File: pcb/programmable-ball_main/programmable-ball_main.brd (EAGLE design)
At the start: 30.5 x 30.8 mm, 2 parts, among them J1 USB4125-GF-A_REVA2, U1 MDBT50Q-1MV2

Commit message: 軽微な修正
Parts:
- J1: value USB4125-GF-A_REVA2 -> USB4056-03-A_REVA2; device USB4125-GF-A_REVA2:GCT_USB4125-GF-A_REVA2 -> USB4056-03-A_REVA2:GCT_USB4056-03-A_REVA2
- moved J1 1.10 mm to (15.0, 2.00)
- moved U1 1.00 mm to (15.0, 19.0)
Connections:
- new net GND_A: J1.A1, J1.A12
- new net GND_B: J1.B1, J1.B12
- new net SHELL_GND: J1.S1, J1.S2, J1.S3, J1.S4
- new net USBD+: U1.35
- new net USBD-: U1.34
- new net VBUS_A: J1.A4, J1.A9
- new net VBUS_B: J1.B4, J1.B9
- net GND: no longer J1.A12, J1.B12
- net VBUS: no longer J1.A9, J1.B9
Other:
- board size 30.5 x 30.8 mm -> 40 x 40 mm
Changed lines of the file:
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@@
 <board>
 <plain>
-<wire x1="0" y1="0" x2="30.51" y2="0" width="0" layer="20"/>
-<wire x1="0" y1="30.77" x2="0" y2="0" width="0" layer="20"/>
+<wire x1="0" y1="30.77" x2="-2" y2="33" width="0" layer="20"/>
 <dimension x1="0" y1="0" x2="0" y2="30" x3="-6" y3="15" textsize="1.778" layer="47"/>
 <dimension x1="0" y1="0" x2="30" y2="0" x3="15" y3="-6" textsize="1.778" layer="47"/>
-<circle x="15" y="15" radius="15" width="0.1524" layer="20"/>
+<circle x="14" y="16" radius="20" width="1" layer="20"/>
+<circle x="4" y="16" radius="1" width="0.1524" layer="20"/>
+<circle x="5" y="11" radius="2.828425" width="0.1524" layer="20"/>
+<circle x="7" y="18" radius="1" width="0.1524" layer="20"/>
+<circle x="4" y="23" radius="1" width="0.1524" layer="20"/>
+<circle x="5" y="20" radius="1" width="0.1524" layer="20"/>
+<circle x="24" y="23" radius="1.4142125" width="0.1524" layer="20"/>
 </plain>
 <attributes>
@@
 </autorouter>
 <elements>
-<element name="U1" library="MDBT50Q-1MV2" package="XCVR_MDBT50Q-1MV2" value="MDBT50Q-1MV2" x="15" y="18" smashed="yes">
-<attribute name="AVAILABILITY" value="In Stock" x="15" y="18" size="1.778" layer="27" display="off"/>
-<attribute name="CHECK_PRICES" value="https://www.snapeda.com/parts/MDBT50Q-1MV2/Raytac+Corporation/view-part/?ref=eda" x="15" y="18" size="1.778" layer="27" display="off"/>
-<attribute name="DESCRIPTION" value=" 802.15.4, Bluetooth Bluetooth v5.2, Zigbee® Transceiver Module 2.36GHz ~ 2.5GHz Integrated, Chip Surface Mount " x="15" y="18" size="1.778" layer="27" display="off"/>
-<attribute name="MF" value="Raytac Corporation" x="15" y="18" size="1.778" layer="27" display="off"/>
-<attribute name="MP" value="MDBT50Q-1MV2" x="15" y="18" size="1.778" layer="27" display="off"/>
-<attribute name="NAME" x="9.75" y="26.19" size="1.27" layer="25"/>
-<attribute name="PACKAGE" value="SMD-61 Raytac Corporation" x="15" y="18" size="1.778" layer="27" display="off"/>
-<attribute name="PRICE" value="None" x="15" y="18" size="1.778" layer="27" display="off"/>
-<attribute name="SNAPEDA_LINK" value="https://www.snapeda.com/parts/MDBT50Q-1MV2/Raytac+Corporation/view-part/?ref=snap" x="15" y="18" size="1.778" layer="27" display="off"/>
+<element name="U1" library="MDBT50Q-1MV2" package="XCVR_MDBT50Q-1MV2" value="MDBT50Q-1MV2" x="15" y="19" smashed="yes">
+<attribute name="AVAILABILITY" value="In Stock" x="15" y="19" size="1.778" layer="27" display="off"/>
+<attribute name="CHECK_PRICES" value="https://www.snapeda.com/parts/MDBT50Q-1MV2/Raytac+Corporation/view-part/?ref=eda" x="15" y="19" size="1.778" layer="27" display="off"/>
+<attribute name="DESCRIPTION" value=" 802.15.4, Bluetooth Bluetooth v5.2, Zigbee® Transceiver Module 2.36GHz ~ 2.5GHz Integrated, Chip Surface Mount " x="15" y="19" size="1.778" layer="27" display="off"/>
+<attribute name="MF" value="Raytac Corporation" x="15" y="19" size="1.778" layer="27" display="off"/>
+<attribute name="MP" value="MDBT50Q-1MV2" x="15" y="19" size="1.778" layer="27" display="off"/>
+<attribute name="NAME" x="9.75" y="27.19" size="1.27" layer="25"/>
+<attribute name="PACKAGE" value="SMD-61 Raytac Corporation" x="15" y="19" size="1.778" layer="27" display="off"/>
+<attribute name="PRICE" value="None" x="15" y="19" size="1.778" layer="27" display="off"/>
+<attribute name="SNAPEDA_LINK" value="https://www.snapeda.com/parts/MDBT50Q-1MV2/Raytac+Corporation/view-part/?ref=snap" x="15" y="19" size="1.778" layer="27" display="off"/>
 </element>
-<element name="J1" library="USB4125-GF-A_REVA2" package="GCT_USB4125-GF-A_REVA2" value="USB4125-GF-A_REVA2" x="15" y="3.1" smashed="yes">
-<attribute name="DESCRIPTION" value=" USB Charge Only Connector Type C Horizontal Receptacle, 3.16mm profile, 6 Pins, Surface mount, Top mount, low cost " x="15" y="3.1" size="1.778" layer="27" display="off"/>
-<attribute name="DIGI-KEY_PART_NUMBER" value="2073-USB4125-GF-ATR-ND" x="15" y="3.1" size="1.778" layer="27" display="off"/>
-<attribute name="MF" value="Global Connector Technology" x="15" y="3.1" size="1.778" layer="27" display="off"/>
-<attribute name="MP" value="USB4125-GF-A" x="15" y="3.1" size="1.778" layer="27" display="off"/>
-<attribute name="NAME" x="11.7" y="7.6" size="1.27" layer="25"/>
-<attribute name="PACKAGE" value="None" x="15" y="3.1" size="1.778" layer="27" display="off"/>
-<attribute name="PURCHASE-URL" value="https://pricing.snapeda.com/search/part/USB4125-GF-A/?ref=eda" x="15" y="3.1" size="1.778" layer="27" display="off"/>
+<element name="J1" library="USB4056-03-A_REVA2" package="GCT_USB4056-03-A_REVA2" value="USB4056-03-A_REVA2" x="15" y="2" smashed="yes">
+<attribute name="AVAILABILITY" value="In Stock" x="15" y="2" size="1.778" layer="27" display="off"/>
+<attribute name="CHECK_PRICES" value="https://www.snapeda.com/parts/USB4056-03-A/Global+Connector+Technology/view-part/?ref=eda" x="15" y="2" size="1.778" layer="27" display="off"/>
+<attribute name="DESCRIPTION" value=" USB-C (USB TYPE-C) USB 3.2 Gen 2 (USB 3.1 Gen 2, Superspeed + (USB 3.1)) Receptacle Connector 24 Position Surface Mount, Right Angle; Through Hole " x="15" y="2" size="1.778" layer="27" display="off"/>
+<attribute name="MF" value="Global Connector Technology" x="15" y="2" size="1.778" layer="27" display="off"/>
+<attribute name="MP" value="USB4056-03-A" x="15" y="2" size="1.778" layer="27" display="off"/>
+<attribute name="PACKAGE" value="None" x="15" y="2" size="1.778" layer="27" display="off"/>
+<attribute name="PRICE" value="None" x="15" y="2" size="1.778" layer="27" display="off"/>
+<attribute name="SNAPEDA_LINK" value="https://www.snapeda.com/parts/USB4056-03-A/Global+Connector+Technology/view-part/?ref=snap" x="15" y="2" size="1.778" layer="27" display="off"/>
 </element>
 </elements>
@@
 <contactref element="U1" pad="33"/>
 <contactref element="U1" pad="2"/>
-<contactref element="J1" pad="B12"/>
-<contactref element="J1" pad="A12"/>
-<wire x1="10.35" y1="21.75" x2="19.65" y2="21.75" width="0" layer="19" extent="1-1"/>
-<wire x1="10.35" y1="20.65" x2="10.35" y2="21.75" width="0" layer="19" extent="1-1"/>
-<wire x1="10.2" y1="10.85" x2="10.35" y2="20.65" width="0" layer="19" extent="1-1"/>
-<wire x1="19.8" y1="10.85" x2="10.2" y2="10.85" width="0" layer="19" extent="1-1"/>
-<wire x1="17.75" y1="6.18" x2="10.2" y2="10.85" width="0" layer="19" extent="1-1"/>
-<wire x1="12.25" y1="6.18" x2="17.75" y2="6.18" width="0" layer="19" extent="1-1"/>
+<wire x1="10.35" y1="22.75" x2="19.65" y2="22.75" width="0" layer="19" extent="1-1"/>
+<wire x1="10.35" y1="21.65" x2="10.35" y2="22.75" width="0" layer="19" extent="1-1"/>
+<wire x1="10.2" y1="11.85" x2="10.35" y2="21.65" width="0" layer="19" extent="1-1"/>
+<wire x1="19.8" y1="11.85" x2="10.2" y2="11.85" width="0" layer="19" extent="1-1"/>
 </signal>
 <signal name="VDDH">
@@
 <signal name="VBUS">
 <contactref element="U1" pad="32"/>
-<contactref element="J1" pad="B9"/>
-<contactref element="J1" pad="A9"/>
-<wire x1="16.52" y1="6.18" x2="19" y2="10.85" width="0" layer="19" extent="1-1"/>
-<wire x1="13.48" y1="6.18" x2="16.52" y2="6.18" width="0" layer="19" extent="1-1"/>
 </signal>
 <signal name="DCCH">
@@
 <contactref element="U1" pad="28"/>
 </signal>
+<signal name="USBD+">
+<contactref element="U1" pad="35"/>
+</signal>
+<signal name="USBD-">
+<contactref element="U1" pad="34"/>
+</signal>
+<signal name="GND_A">
+<contactref element="J1" pad="A12"/>
+<contactref element="J1" pad="A1"/>
+<wire x1="17.75" y1="8.2" x2="12.25" y2="8.2" width="0" layer="19" extent="1-1"/>
+</signal>
+<signal name="VBUS_A">
+<contactref element="J1" pad="A4"/>
+<contactref element="J1" pad="A9"/>
+<wire x1="16.25" y1="8.2" x2="13.75" y2="8.2" width="0" layer="19" extent="1-1"/>
+</signal>
+<signal name="SHELL_GND">
+<contactref element="J1" pad="S2"/>
+<contactref element="J1" pad="S1"/>
+<contactref element="J1" pad="S4"/>
+<contactref element="J1" pad="S3"/>
+<wire x1="10.87" y1="6.4" x2="10.51" y2="2" width="0" layer="19" extent="1-1"/>
+<wire x1="19.13" y1="6.4" x2="10.87" y2="6.4" width="0" layer="19" extent="1-1"/>
+<wire x1="19.49" y1="2" x2="19.13" y2="6.4" width="0" layer="19" extent="1-1"/>
+</signal>
+<signal name="GND_B">
+<contactref element="J1" pad="B12"/>
+<contactref element="J1" pad="B1"/>
+<wire x1="17.8" y1="6.99" x2="12.2" y2="6.99" width="0" layer="19" extent="1-1"/>
+</signal>
+<signal name="VBUS_B">
+<contactref element="J1" pad="B9"/>
+<contactref element="J1" pad="B4"/>
+<wire x1="16.2" y1="6.99" x2="13.8" y2="6.99" width="0" layer="19" extent="1-1"/>
+</signal>
 </signals>

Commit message: usb typeC周り実装 #4
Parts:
- added R1, R2: 5.1k, SparkFun-Resistors:0402-TIGHT
- J1: value USB4056-03-A_REVA2 -> 12402012E212A; device USB4056-03-A_REVA2:GCT_USB4056-03-A_REVA2 -> 12402012E212A:AMPHENOL_12402012E212A
- moved J1 2.50 mm to (15.0, 4.50)
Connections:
- removed net GND_A: J1.A1, J1.A12
- removed net GND_B: J1.B1, J1.B12
- removed net SHELL_GND: J1.S1, J1.S2, J1.S3, J1.S4
- removed net VBUS_A: J1.A4, J1.A9
- removed net VBUS_B: J1.B4, J1.B9
- new net N$1: J1.A5, R1.2
- new net N$2: J1.B5, R2.2
- net GND: now also J1.A1_B12, J1.B1_A12, R1.1, R2.1
- net USBD+: now also J1.A6, J1.B6
- net USBD-: now also J1.A7, J1.B7
- net VBUS: now also J1.A4_B9, J1.B4_A9
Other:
- board size 40 x 40 mm -> 27 x 27 mm

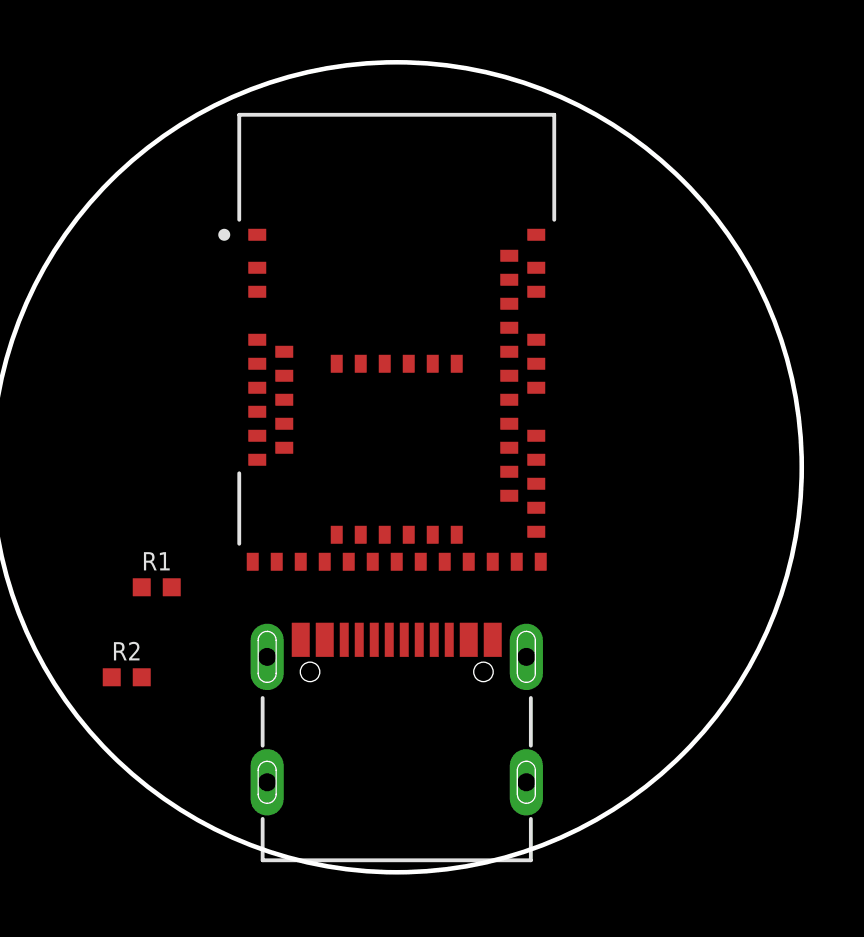
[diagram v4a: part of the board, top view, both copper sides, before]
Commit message: スイッチを追加 #4
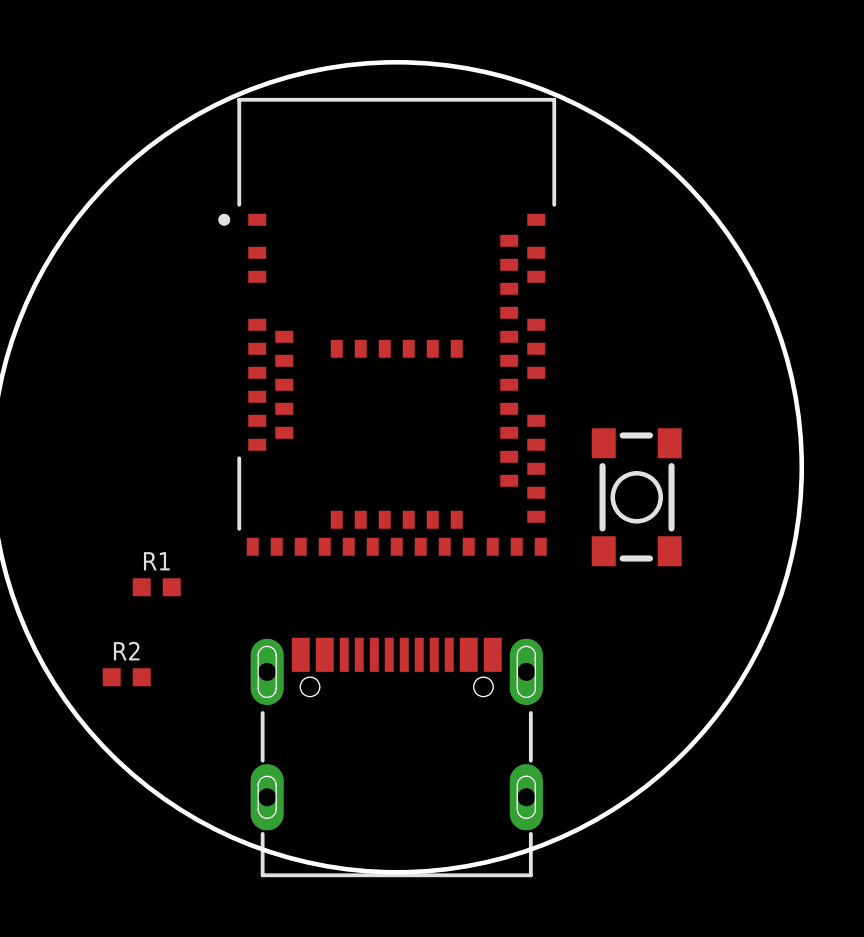
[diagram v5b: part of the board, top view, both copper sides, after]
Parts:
- added S1: SWITCH-MOMENTARY-SPSTSMD-3, SparkFun-Retired:TACTILE_SWITCH_SMD-3
- moved J1 0.50 mm to (15.0, 4.00)
- moved U1 0.50 mm to (15.0, 19.5)
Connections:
- new net I2C_SCL: U1.49
- new net I2C_SDA: U1.19
- new net RESET: S1.4, U1.40
- new net SWDCLK: U1.53
- new net SWDIO: U1.51
- net GND: now also S1.1

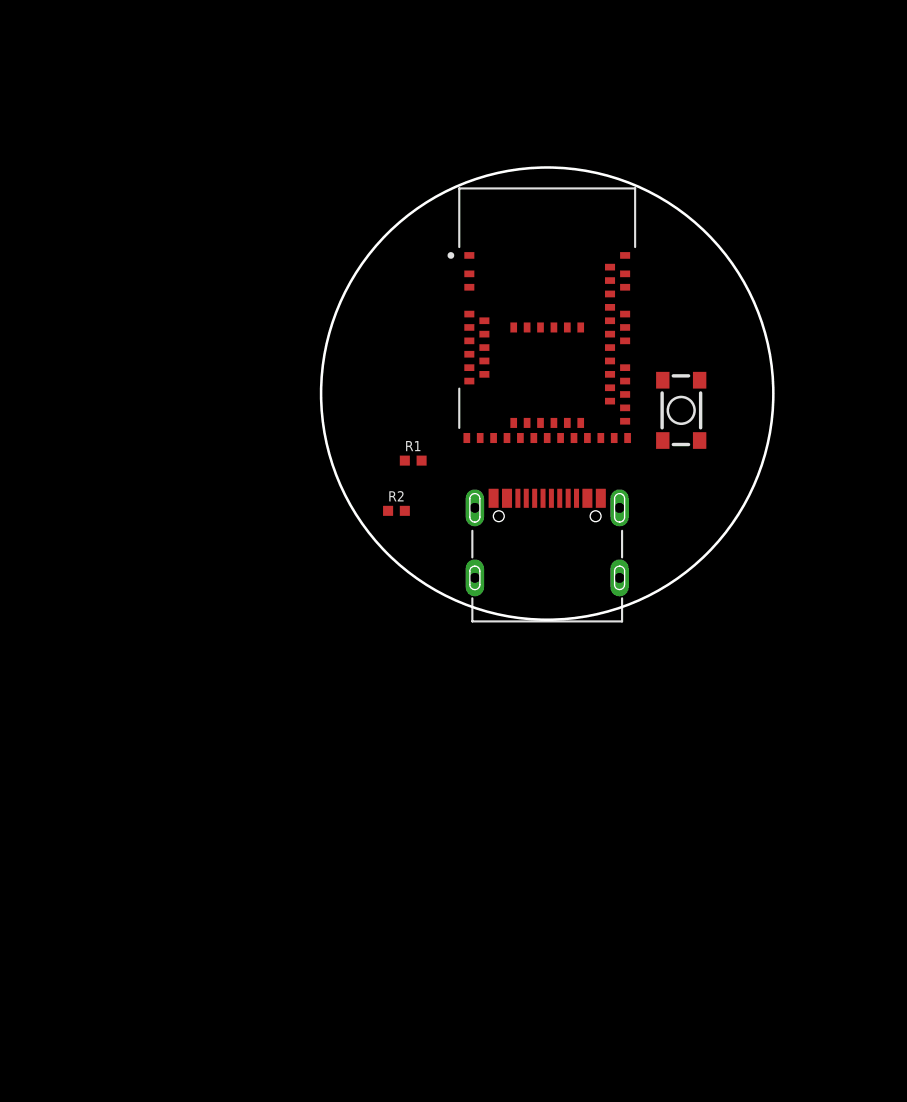
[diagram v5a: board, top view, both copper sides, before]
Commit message: 3.3VのレギュレータとVBATよりVBUSを優先するように修正
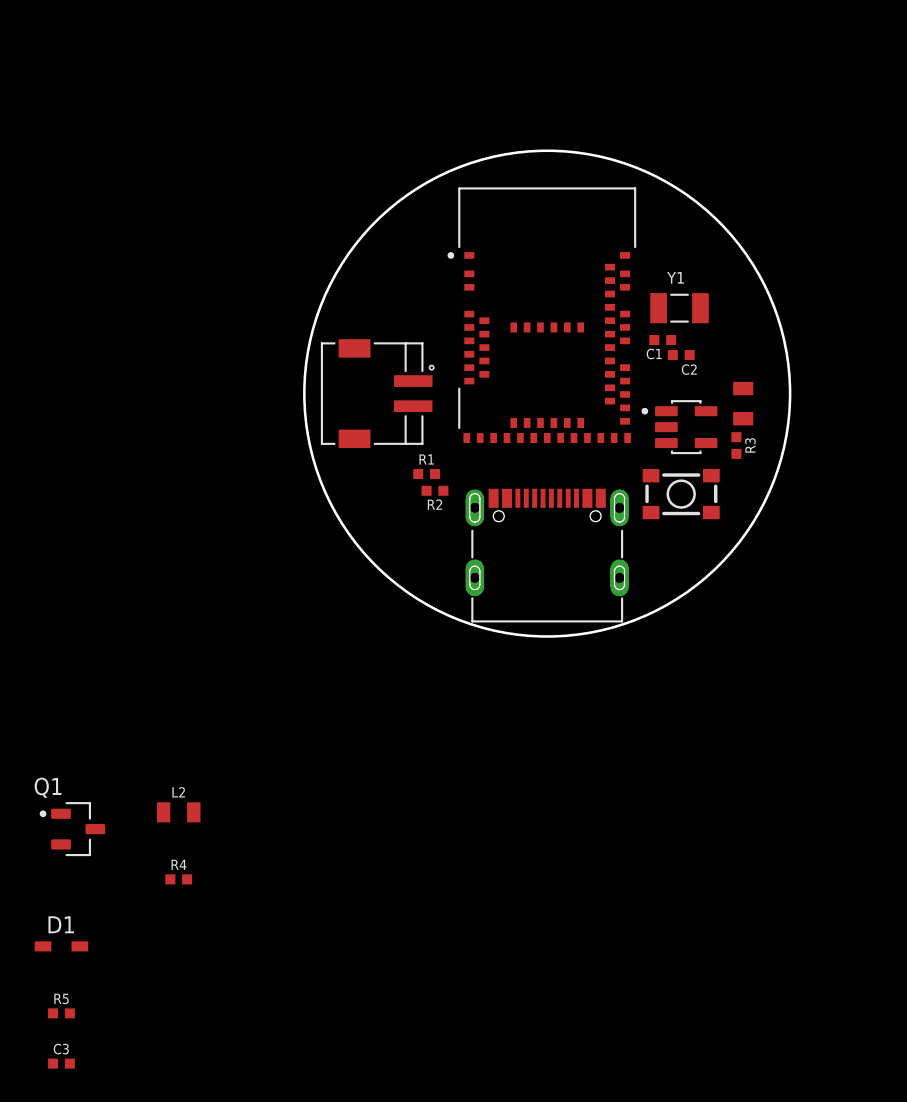
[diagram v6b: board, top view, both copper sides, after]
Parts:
- added C1, C2: 9.1pF, SparkFun-Capacitors:0402-TIGHT
- added C3: 10uF, SparkFun-Capacitors:0402-TIGHT
- added D1: MBR120LSFT1G, zetex:SOD323
- added L1: DNP, SparkFun-Coils:0805
- added L2: 10μH, SparkFun-Coils:0805
- added P1: S2B-ZR-SM4A-TF, S2B-ZR-SM4A-TF:JST_S2B-ZR-SM4A-TF
- added Q1: DMG2305UX-13, DMG2305UX-13:SOT91P240X110-3N
- added R3: 47k, SparkFun-Resistors:0402-TIGHT
- added R4, R5: 100k, SparkFun-Resistors:0402-TIGHT
- added U2: AP2112K-3.3TRG1, AP2112K-3.3TRG1:SOT95P285X140-5N
- added Y1: FC-135_32.7680KA-A0, FC-135_32.7680KA-A0:XTAL_FC-135_32.7680KA-A0
- moved S1 5.00 mm to (23.0, 9.00), turned to 0 degrees
- moved R2 2.59 mm to (8.30, 9.20)
- moved R1 1.13 mm to (7.80, 10.2)
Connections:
- removed net DCCH: U1.31
- removed net VDD: U1.28
- removed net VDDH: U1.30
- new net 3.3V: L1.1, L2.1, R3.2, U1.28, U1.30, U2.5
- new net N$3: C2.1, U1.18, Y1.2
- new net N$4: C1.1, U1.17, Y1.1
- new net N$5: L1.2, U1.31
- new net N$6: C3.2, D1.1, Q1.2, R4.2, U2.1
- new net N$7: R4.1, U2.3
- new net VBAT: P1.1, Q1.3
- net GND: now also C1.2, C2.2, C3.1, L2.2, P1.2, R5.1, U2.2
- net RESET: now also R3.1
- net VBUS: now also D1.2, Q1.1, R5.2
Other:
- board size 27 x 27 mm -> 29 x 29 mm

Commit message: スライドスイッチを追加 #4
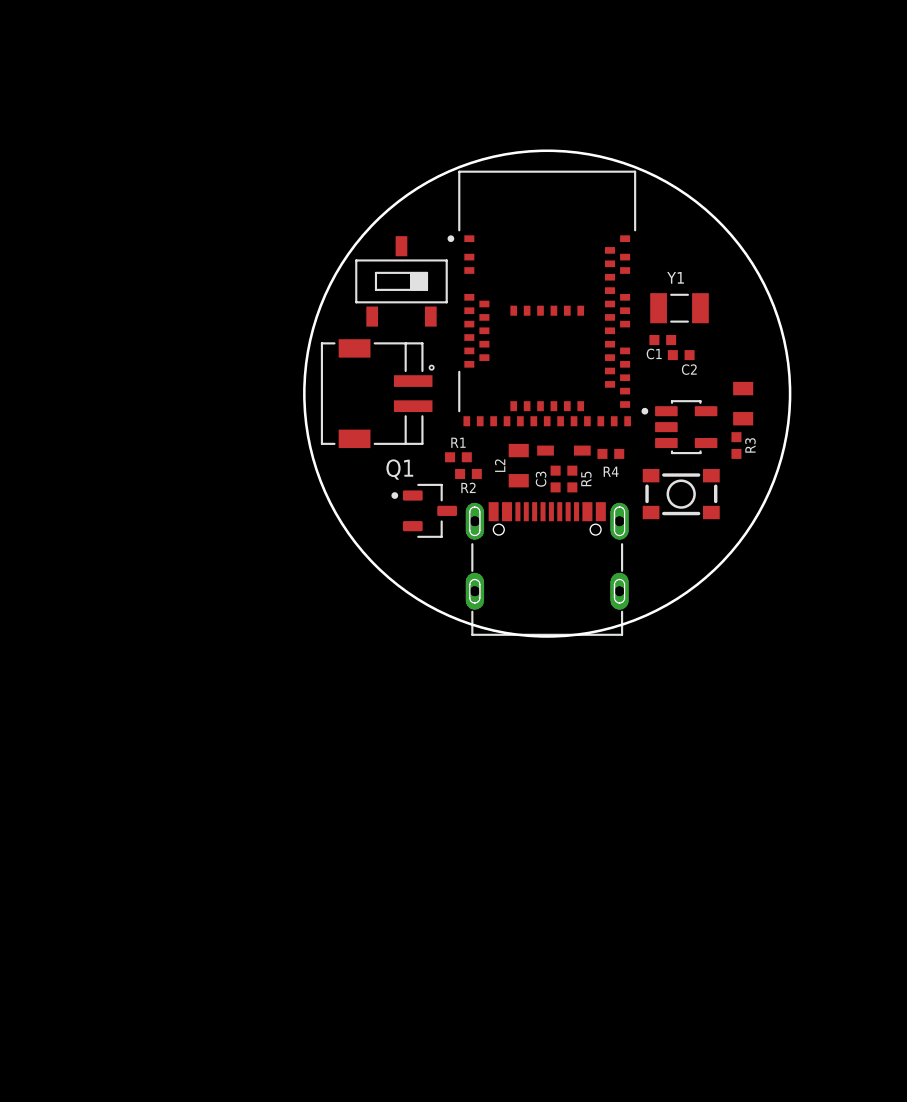
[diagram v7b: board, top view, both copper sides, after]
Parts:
- added SW1: CAS-120CAS-120B1, Switch:CAS-120B1
- moved C3 45.7 mm to (15.5, 9.90), turned to 90 degrees
- moved R5 44.1 mm to (16.5, 9.90), turned to 90 degrees
- moved D1 42.1 mm to (16.0, 11.6)
- moved R4 36.2 mm to (18.8, 11.4), turned to 180 degrees
- moved L2 29.0 mm to (13.3, 10.7), turned to 270 degrees
- moved Q1 28.3 mm to (8.00, 8.00)
- moved R2 2.24 mm to (10.3, 10.2)
- moved R1 2.15 mm to (9.70, 11.2)
- moved U1 1.00 mm to (15.0, 20.5)
- moved J1 0.80 mm to (15.0, 3.20)
